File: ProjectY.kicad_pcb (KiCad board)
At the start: 4 copper layers, 192 parts, among them J10 NRJ6HF, J11 NRJ6HF, J2 NRJ6HF, J3 9V, J4 NRJ6HF, J5 NRJ6HF, J6 NRJ6HF, J8 Midi In, J9 MIDI Out, P1 USB_C, Q1 DMT6008LFG, Q2 BC847BS, Q3 BC846BS, Q4 BC856BS, U1 W9825G6KH-6, U10 OPA1692xDGK, U12 USBLC6-2P6, U13 OPA2156xD, U14 OPA1692xDGK, U15 ISOM8115, U16 OPA2156xD, U17 TPS2121RUXR, U18 STM32H7R7I8Tx, U19 TLV77333PDBVR, U20 TPS65133DPDR, U21 LM74700, U22 TLV77325PDBVR, U23 OPA2156xD, U3 FM24CL64B, U4 TPS7A39, U5 OPA2156xD, U6 TAC5242, U7 OPA2156xD, U8 OPA2156xD, U9 OPA2156xD, Y1 ASDLJ-E-49.152MHZ-L-R-T

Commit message: started the layout process
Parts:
- removed C80: 1uF, PCM_JLCPCB:C_0402
- removed D10, D9: BAT54WS, PCM_JLCPCB:D_SOD-323
- removed J11: NRJ6HF, Connector_Audio:Jack_6.35mm_Neutrik_NRJ6HF_Horizontal
- removed P1: USB_C, Connector_USB:USB_C_Receptacle_GCT_USB4110
- removed Q2: BC847BS, PCM_JLCPCB:SOT-363_SC-70-6
- removed Q3: BC846BS, Package_TO_SOT_SMD:SOT-363_SC-70-6
- removed Q4: BC856BS, Package_TO_SOT_SMD:SOT-363_SC-70-6
- added C100: 100nF, PCM_JLCPCB:C_0402, F.Cu at (114.5, 71.4)
- added C101: 100nF, PCM_JLCPCB:C_0402, F.Cu at (114.4, 75.1)
- added C102: 100nF, PCM_JLCPCB:C_0402, F.Cu at (117.8, 75.5)
- added C103: 100nF, PCM_JLCPCB:C_0402, F.Cu at (117.8, 71.2)
- added C104: 100nF, PCM_JLCPCB:C_0402, F.Cu at (111.7, 88.3)
- added C105: 100nF, PCM_JLCPCB:C_0402, F.Cu at (111.7, 92.1)
- added C106: 100uF, PCM_JLCPCB:C_1206, F.Cu at (33.7, 113.6)
- added C107: 100uF, PCM_JLCPCB:C_1206, F.Cu at (33.7, 108.9)
- added C108: 100uF, PCM_JLCPCB:C_1206, F.Cu at (31.3, 108.9)
- added C109: 100uF, PCM_JLCPCB:C_1206, F.Cu at (31.3, 113.6)
- added C110: 100uF, PCM_JLCPCB:C_1206, F.Cu at (28.8, 108.9)
- added C111: 100uF, PCM_JLCPCB:C_1206, F.Cu at (28.8, 113.6)
- added C112: 2.2uF, PCM_JLCPCB:C_0402, F.Cu at (180.6, 162.3)
- added C113: 2.2uF, PCM_JLCPCB:C_0402, F.Cu at (163.2, 165.6)
- added C114: 2.2uF, PCM_JLCPCB:C_0402, F.Cu at (180.7, 143.9)
- added C115: 2.2uF, PCM_JLCPCB:C_0402, F.Cu at (160.3, 136.1)
- added C116: 1uF, PCM_JLCPCB:C_0402, F.Cu at (170.5, 135.6)
- added C117: 100nF, PCM_JLCPCB:C_0402, F.Cu at (170.5, 136.5)
- added C118: 1uF, PCM_JLCPCB:C_0402, F.Cu at (150.7, 139.6)
- added C119: 100nF, PCM_JLCPCB:C_0402, F.Cu at (151.7, 139.6)
- added C120: 4.7uF, PCM_JLCPCB:C_0402, F.Cu at (158.5, 136.1)
- added C121: 100nF, PCM_JLCPCB:C_0402, F.Cu at (161.4, 165.6)
- added C122: 100nF, PCM_JLCPCB:C_0402, F.Cu at (158.2, 165.6)
- added C123: 100nF, PCM_JLCPCB:C_0402, F.Cu at (151.2, 160.1)
- added C124: 100nF, PCM_JLCPCB:C_0402, F.Cu at (151.2, 153.1)
- added C125: 100nF, PCM_JLCPCB:C_0402, F.Cu at (151.3, 145.7)
- added C126: 100nF, PCM_JLCPCB:C_0402, F.Cu at (151.2, 142.1)
- added C127: 1uF, PCM_JLCPCB:C_0402, F.Cu at (88.7, 121.4)
- added C128: 100nF, PCM_JLCPCB:C_0402, F.Cu at (180.6, 160.5)
- added C130: 100nF, PCM_JLCPCB:C_0402, F.Cu at (180.7, 148.1)
- added C132: 100nF, PCM_JLCPCB:C_0402, F.Cu at (180.7, 142.0)
- added C133: 100nF, PCM_JLCPCB:C_0402, F.Cu at (172.7, 136.1)
- added C134: 100nF, PCM_JLCPCB:C_0402, F.Cu at (88.7, 123.2)
- added C135: 4.7uF, PCM_JLCPCB:C_0402, F.Cu at (172.9, 165.1)
- added C136: 100nF, PCM_JLCPCB:C_0402, F.Cu at (172.9, 166.0)
- added C137: 100nF, PCM_JLCPCB:C_0402, F.Cu at (167.2, 165.1)
- added C138: 100nF, PCM_JLCPCB:C_0402, F.Cu at (164.1, 165.6)
- added C139: 4.7uF, PCM_JLCPCB:C_0402, F.Cu at (180.6, 151.1)
- added C140: 100nF, PCM_JLCPCB:C_0402, F.Cu at (180.6, 159.6)
- added C141: 100nF, PCM_JLCPCB:C_0402, F.Cu at (180.6, 156.6)
- added C142: 100nF, PCM_JLCPCB:C_0402, F.Cu at (180.6, 153.6)
- added C143: 100nF, PCM_JLCPCB:C_0402, F.Cu at (180.7, 142.9)
- added C144: 100nF, PCM_JLCPCB:C_0402, F.Cu at (180.6, 161.4)
- added C145: 100nF, PCM_JLCPCB:C_0402, F.Cu at (159.4, 136.1)
- added C146: 100nF, PCM_JLCPCB:C_0402, F.Cu at (162.3, 165.6)
- added C147: 10uF, PCM_JLCPCB:C_0603, F.Cu at (114.0, 133.0)
- added C148: 4.7uF, PCM_JLCPCB:C_0402, F.Cu at (91.5, 112.2)
- added C149: 2.2uF, PCM_JLCPCB:C_0402, F.Cu at (91.5, 114.0)
- added C150: 2.2uF, PCM_JLCPCB:C_0402, F.Cu at (91.5, 115.8)
- added C151: 2.2uF, PCM_JLCPCB:C_0402, F.Cu at (91.5, 117.7)
- added C152: 2.2uF, PCM_JLCPCB:C_0402, F.Cu at (91.5, 119.5)
- added C153: 10uF, PCM_JLCPCB:C_0603, F.Cu at (114.0, 135.2)
- added C154: 220pF, PCM_JLCPCB:C_0402, F.Cu at (151.3, 146.6)
- added C155: 100nF, PCM_JLCPCB:C_0402, F.Cu at (150.4, 148.1)
- added C53: 100uF, PCM_JLCPCB:C_1206, F.Cu at (38.6, 113.6)
- added C56: 100uF, PCM_JLCPCB:C_1206, F.Cu at (38.6, 108.9)
- added C66: 10nF, PCM_JLCPCB:C_0402, F.Cu at (27.0, 113.1)
- added C67: 100nF, PCM_JLCPCB:C_0402, F.Cu at (185.2, 150.6)
- added C74: 2.2nF, PCM_JLCPCB:C_0805, F.Cu at (119.1, 141.7)
- added C75: 2.2nF, PCM_JLCPCB:C_0805, F.Cu at (119.1, 147.8)
- added C76: 100nF, PCM_JLCPCB:C_0402, F.Cu at (164.7, 136.2)
- added C77: 100nF, PCM_JLCPCB:C_0402, F.Cu at (112.8, 185.9)
- added C88: 100nF, PCM_JLCPCB:C_0402, F.Cu at (85.8, 115.8)
- added C89: 100nF, PCM_JLCPCB:C_0402, F.Cu at (85.8, 117.7)
- added C90: 100nF, PCM_JLCPCB:C_0402, F.Cu at (85.8, 119.5)
- added C91: 100nF, PCM_JLCPCB:C_0402, F.Cu at (85.8, 121.4)
- added C92: 100nF, PCM_JLCPCB:C_0402, F.Cu at (85.8, 123.2)
- added C93: 100nF, PCM_JLCPCB:C_0402, F.Cu at (85.8, 125.1)
- added C94: 100pF, PCM_JLCPCB:C_0402, F.Cu at (39.3, 71.8)
- added C96: 10uF, PCM_JLCPCB:C_0402, F.Cu at (72.2, 192.2)
- added C97: 100nF, PCM_JLCPCB:C_0402, F.Cu at (113.4, 73.3)
- added C98: 100nF, PCM_JLCPCB:C_0402, F.Cu at (110.7, 90.3)
- added C99: 100nF, PCM_JLCPCB:C_0402, F.Cu at (85.8, 134.3)
- added D19: BAV99, Package_TO_SOT_SMD:SOT-23, F.Cu at (43.7, 71.9)
- added D2: SMF6.0CA, PCM_JLCPCB:D_SOD-123FL, F.Cu at (97.9, 168.7)
- added NT1: ~, NetTie:NetTie-2_SMD_Pad0.5mm, F.Cu at (115.9, 156.4)
- added NT10: ~, NetTie:NetTie-2_SMD_Pad0.5mm, F.Cu at (115.9, 168.4)
- added NT3: ~, NetTie:NetTie-2_SMD_Pad0.5mm, F.Cu at (115.9, 157.9)
- added NT4: ~, NetTie:NetTie-2_SMD_Pad0.5mm, F.Cu at (115.9, 159.4)
- added NT5: ~, NetTie:NetTie-2_SMD_Pad0.5mm, F.Cu at (115.9, 160.9)
- added NT6: ~, NetTie:NetTie-2_SMD_Pad0.5mm, F.Cu at (115.9, 162.4)
- added NT7: ~, NetTie:NetTie-2_SMD_Pad0.5mm, F.Cu at (115.9, 163.9)
- added NT8: ~, NetTie:NetTie-2_SMD_Pad0.5mm, F.Cu at (115.9, 165.4)
- added NT9: ~, NetTie:NetTie-2_SMD_Pad0.5mm, F.Cu at (115.9, 166.9)
- added Q6: BC847, Package_TO_SOT_SMD:SOT-23, F.Cu at (104.8, 144.2)
- added Q7: BC847, Package_TO_SOT_SMD:SOT-23, F.Cu at (104.8, 148.8)
- added Q8: BC847, Package_TO_SOT_SMD:SOT-23, F.Cu at (104.8, 153.4)
- added Q9: BC847, Package_TO_SOT_SMD:SOT-23, F.Cu at (104.8, 158.0)
- added R100: 10kΩ, PCM_JLCPCB:R_0402, F.Cu at (100.1, 127.0)
- added R101: 1kΩ, PCM_JLCPCB:R_0805, F.Cu at (100.1, 153.3)
- added R102: 1kΩ, PCM_JLCPCB:R_0805, F.Cu at (100.1, 156.3)
- added R103: 10kΩ, PCM_JLCPCB:R_0402, F.Cu at (100.1, 128.8)
- added R104: 100Ω, PCM_JLCPCB:R_0402, F.Cu at (115.8, 70.7)
- added R105: 100Ω, PCM_JLCPCB:R_0402, F.Cu at (115.8, 76.0)
- added R106: 100Ω, PCM_JLCPCB:R_0402, F.Cu at (116.7, 76.0)
- added R107: 100Ω, PCM_JLCPCB:R_0402, F.Cu at (116.8, 70.8)
- added R108: 100Ω, PCM_JLCPCB:R_0402, F.Cu at (115.0, 88.5)
- added R109: 100Ω, PCM_JLCPCB:R_0402, F.Cu at (115.0, 92.0)
- added R110: 10kΩ, PCM_JLCPCB:R_0402, F.Cu at (113.4, 72.4)
- added R111: 10kΩ, PCM_JLCPCB:R_0402, F.Cu at (113.4, 74.2)
- added R112: 10kΩ, PCM_JLCPCB:R_0402, F.Cu at (118.7, 73.8)
- added R113: 10kΩ, PCM_JLCPCB:R_0402, F.Cu at (118.7, 72.6)
- added R114: 10kΩ, PCM_JLCPCB:R_0402, F.Cu at (110.7, 89.3)
- added R115: 10kΩ, PCM_JLCPCB:R_0402, F.Cu at (110.7, 91.2)
- added R116: 1kΩ, PCM_JLCPCB:R_0402, F.Cu at (188.4, 146.2)
- added R117: 10kΩ, PCM_JLCPCB:R_0402, F.Cu at (102.9, 128.8)
- added R118: 100Ω, PCM_JLCPCB:R_0402, F.Cu at (32.6, 69.5)
- added R35: 33Ω, PCM_JLCPCB:R_0402, F.Cu at (94.4, 117.7)
- added R40: 33Ω, PCM_JLCPCB:R_0402, F.Cu at (94.4, 125.1)
- added R45: 33Ω, PCM_JLCPCB:R_0402, F.Cu at (94.4, 130.7)
- added R59: R, Resistor_SMD:R_0402_1005Metric, F.Cu at (25.9, 109.2)
- added R61: R, Resistor_SMD:R_0402_1005Metric, F.Cu at (25.9, 113.1)
- added R74: 10kΩ, PCM_JLCPCB:R_0402, F.Cu at (97.2, 119.5)
- added R75: 510Ω, PCM_JLCPCB:R_0805, F.Cu at (158.1, 45.3)
- added R78: 10kΩ, PCM_JLCPCB:R_0402, F.Cu at (97.2, 123.2)
- added R82: 510Ω, PCM_JLCPCB:R_0805, F.Cu at (134.3, 42.9)
- added R83: 510Ω, PCM_JLCPCB:R_0805, F.Cu at (134.3, 45.8)
- added R84: 10kΩ, PCM_JLCPCB:R_0402, F.Cu at (97.2, 127.0)
- added R85: 10kΩ, PCM_JLCPCB:R_0402, F.Cu at (97.2, 130.7)
- added R86: 10kΩ, PCM_JLCPCB:R_0402, F.Cu at (97.2, 134.3)
- added R87: 10kΩ, PCM_JLCPCB:R_0402, F.Cu at (100.1, 112.2)
- added R88: 10kΩ, PCM_JLCPCB:R_0805, F.Cu at (162.8, 23.5)
- added R89: 10kΩ, PCM_JLCPCB:R_0805, F.Cu at (162.8, 27.1)
- added R90: 10kΩ, PCM_JLCPCB:R_0805, F.Cu at (134.3, 48.8)
- added R91: 10kΩ, PCM_JLCPCB:R_0805, F.Cu at (134.3, 51.7)
- added R92: 10kΩ, PCM_JLCPCB:R_0402, F.Cu at (100.1, 115.8)
- added R93: 10kΩ, PCM_JLCPCB:R_0402, F.Cu at (100.1, 117.7)
- added R94: 10kΩ, PCM_JLCPCB:R_0402, F.Cu at (100.1, 119.5)
- added R95: 10kΩ, PCM_JLCPCB:R_0402, F.Cu at (100.1, 121.4)
- added R96: 10kΩ, PCM_JLCPCB:R_0402, F.Cu at (100.1, 123.2)
- added R97: 10kΩ, PCM_JLCPCB:R_0402, F.Cu at (100.1, 125.1)
- added R99: 1MΩ, PCM_JLCPCB:R_0805, F.Cu at (40.8, 72.5)
- added U2: W25Q128JVS, Package_SO:SOIC-8_5.3x5.3mm_P1.27mm, F.Cu at (167.2, 170.5)
- added U24: OPA1692xDGK, Package_SO:VSSOP-8_3x3mm_P0.65mm, F.Cu at (86.6, 34.0)
- added U25: TLV9004xRUCR, Package_DFN_QFN:Texas_S-PX2QFN-14, F.Cu at (116.0, 73.4)
- added U26: TLV9004xRUCR, Package_DFN_QFN:Texas_S-PX2QFN-14, F.Cu at (113.4, 90.3)
- added U27: TLV77333PDBVR, Package_TO_SOT_SMD:SOT-23-5, F.Cu at (69.5, 192.5)
- C53, C56: footprint PCM_JLCPCB:C_CASE-B-3528-21(mm) -> PCM_JLCPCB:C_1206
- C6: footprint PCM_JLCPCB:C_0603 -> PCM_JLCPCB:C_0402
- C74, C75: value 1uF -> 2.2nF; footprint PCM_JLCPCB:C_0402 -> PCM_JLCPCB:C_0805
- C76, C77: value 1uF -> 100nF
- C78: value 1uF -> 10uF
- C79: value 1uF -> 10nF
- J2: value NRJ6HF -> Conn_ARM_JTAG_SWD_10; footprint Connector_Audio:Jack_6.35mm_Neutrik_NRJ6HF_Horizontal -> Connector_PinHeader_1.27mm:PinHeader_2x05_P1.27mm_Vertical_SMD
- J9: value MIDI Out -> USB_C_Receptacle_USB2.0_14P; footprint Connector_Audio:Jack_3.5mm_Lumberg_1503_07_Horizontal -> Connector_USB:USB_C_Receptacle_GCT_USB4110
- R13, R14, R16, R80, R81: footprint PCM_JLCPCB:R_0805 -> PCM_JLCPCB:R_0402
- R2: value 1MΩ -> 220Ω; footprint PCM_JLCPCB:R_0402 -> PCM_JLCPCB:R_0805
- R30: value 120Ω -> 100kΩ
- R35: value 120Ω -> 33Ω
- R4: value 1MΩ -> 100kΩ
- R40, R45: value 10kΩ -> 33Ω
- R74, R78: value 1kΩ -> 10kΩ; footprint PCM_JLCPCB:R_0805 -> PCM_JLCPCB:R_0402
- R75, R79: value 1kΩ -> 510Ω
- R84, R85, R86, R87: value 100kΩ -> 10kΩ; footprint PCM_JLCPCB:R_0805 -> PCM_JLCPCB:R_0402
- U1: moved to B.Cu
- U13, U16, U23, U5, U8, U9: footprint Package_SO:SOIC-8_3.9x4.9mm_P1.27mm -> Package_SO:VSSOP-8_3x3mm_P0.65mm
- U7: value OPA2156xD -> 74HC14
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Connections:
- net /Analog Audio/IN_R+ renamed /IN_R+
- net /Analog Audio/IN_R- renamed /IN_R-
- net /Analog Audio/Line_Output_L+ renamed /Line_Output_L+
- net /Analog Audio/Line_Output_L- renamed /Line_Output_L-
- net /Analog Audio/~{Dry_Through} renamed /Analog Audio/Dry_Through
- net /Analog Audio/~{Hi-Z} renamed /Analog Audio/Hi-Z
- net Net-(K2-Pad3) renamed Processing_In_Right
- net Net-(K2-Pad6) renamed Processing_In_Left
- net Net-(R18-Pad2) renamed Processing_Inverted_Right
- net Net-(R22-Pad1) renamed Processing_Inverted_Left
- net Net-(U5B--) renamed Summing_In_L
- net Net-(U9A--) renamed Unbal_Left
- net Net-(U9B--) renamed Unbal_Right
- C38 pad 1: Net-(U7A-+) -> Net-(U24A-+)
- C38 pad 2: Net-(U7A--) -> Net-(U24A--)
- C39 pad 1: Net-(U7A-+) -> Net-(U24A-+)
- C39 pad 2: Net-(U7A--) -> Net-(U24A--)
- C44 pad 1: Net-(U7B-+) -> Net-(U24B-+)
- C44 pad 2: Net-(U7B--) -> Net-(U24B--)
- C45 pad 1: Net-(U7B-+) -> Net-(U24B-+)
- C45 pad 2: Net-(U7B--) -> Net-(U24B--)
- C53 pad 1: /Analog Audio/+4.5V -> GND
- C53 pad 2: GND -> /Analog Audio/-4.5V
- C56 pad 1: GND -> /Analog Audio/+4.5V
- C56 pad 2: /Analog Audio/-4.5V -> GND
- C69 pad 1: /PSU/+2.5VA -> /DSP/2.5V_VREF
- C74 pad 1: /MIDI + UI/MIDI IN Shield -> GND
- C74 pad 2: GND -> /Line_Output_R+
- C75 pad 1: /MIDI + UI/MIDI IN Shield -> GND
- C75 pad 2: GND -> /Line_Output_R-
- C76 pad 1: /MIDI + UI/MIDI IN Shield -> VDD
- C77 pad 1: /MIDI + UI/MIDI OUT Shield -> VDD
- C78 pad 1: /MIDI + UI/MIDI OUT Shield -> /PSU/+5V
- C79 pad 1: /MIDI + UI/MIDI OUT Shield -> /Analog Audio/+4.5V
- C79 pad 2: GND -> FBP
- D11 pad 3: /Analog Audio/Guitar_IN -> Buffer_In_Left
- D14 pad 3: /Analog Audio/Line_Output_R+ -> /Line_Output_R+
- D15 pad 3: /Analog Audio/Line_Output_R- -> /Line_Output_R-
- D16 pad 3: /Analog Audio/IN_L+ -> Balun_In_Left+
- D8 pad 3: /Analog Audio/IN_L- -> Balun_In_Left-
- J4 pad R: /Analog Audio/Line_Output_R- -> /Line_Output_R-
- J4 pad T: /Analog Audio/Line_Output_R+ -> /Line_Output_R+
- J6 pad R: /Analog Audio/IN_L- -> /IN_L-
- J6 pad T: /Analog Audio/IN_L+ -> /IN_L+
- R13 pad 1: /Analog Audio/Guitar_IN -> Buffer_In_Right
- R13 pad 2: Net-(U9A-+) -> Net-(U9B-+)
- R14 pad 1: /Analog Audio/IN_L- -> Balun_In_Left-
- R16 pad 1: /Analog Audio/IN_L+ -> Balun_In_Left+
- R2 pad 1: /MIDI + UI/MIDI IN Shield -> /MIDI + UI/Midi In Sink
- R2 pad 2: GND -> Net-(R2-Pad2)
- R26 pad 2: Net-(U7A--) -> Net-(U24A--)
- R27 pad 2: Net-(U7A-+) -> Net-(U24A-+)
- R28 pad 2: Net-(U7B--) -> Net-(U24B--)
- R29 pad 2: Net-(U7B-+) -> Net-(U24B-+)
- R30 pad 1: Net-(Q3A-E1) -> +3.3VA2_Midpoint
- R35 pad 1: /Analog Audio/+3.3V -> Net-(U18-PA13(JTMS)
- R35 pad 2: Net-(Q4A-E1) -> /DSP/SWDIO
- R4 pad 1: /MIDI + UI/MIDI OUT Shield -> /MIDI + UI/+3.3VA2
- R4 pad 2: GND -> +3.3VA2_Midpoint
- R40 pad 1: Net-(Q4A-B1) -> Net-(U18-PA14(JTCK)
- R40 pad 2: GND -> /DSP/SWCLK
- R45 pad 1: /DSP/MIDI_UART0_TX -> Net-(U18-PB3(JTDO)
- R45 pad 2: Net-(Q3A-B1) -> /DSP/SWO
- R74 pad 1: GND -> /Analog Audio/+3.3V
- R74 pad 2: Net-(U16B-+) -> Net-(J1-Pin_1)
- R75 pad 1: GND -> Net-(U16A--)
- R75 pad 2: Net-(U16A-+) -> Balun_Left
- R78 pad 1: Net-(U16B--) -> Net-(J1-Pin_1)
- R78 pad 2: Net-(K2-Pad4) -> Net-(C88-Pad1)
- R79 pad 1: Net-(U16A--) -> GND
- R79 pad 2: Net-(K2-Pad5) -> Net-(U16A-+)
- R84 pad 1: Net-(U13A-+) -> /Analog Audio/+3.3V
- R84 pad 2: GND -> Net-(J12-Pin_1)
- R85 pad 1: GND -> Net-(J12-Pin_1)
- R85 pad 2: Net-(U13B-+) -> Net-(C89-Pad1)
- R86 pad 1: Net-(U23A-+) -> /Analog Audio/+3.3V
- R86 pad 2: GND -> Net-(J13-Pin_1)
- R87 pad 1: GND -> Net-(J13-Pin_1)
- R87 pad 2: Net-(U23B-+) -> Net-(C90-Pad1)
- U1 pad 12: GNDD -> GND
- U1 pad 28: GNDD -> GND
- U1 pad 41: GNDD -> GND
- U1 pad 46: GNDD -> GND
- U1 pad 52: GNDD -> GND
- U1 pad 54: GNDD -> GND
- U1 pad 6: GNDD -> GND
- U15 pad 2: /MIDI + UI/Midi In Sink -> Net-(R2-Pad2)
- U16 pad 1: Net-(K2-Pad5) -> Balun_Left
- U16 pad 7: Net-(K2-Pad4) -> Balun_Right
- U18 pad 1: /DSP/VTREF -> VBAT
- U18 pad 105: unconnected-(U18-VDDXSPI2-Pad105) -> VDDXSPI2
- U18 pad 110: unconnected-(U18-VDDXSPI2-Pad110) -> VDDXSPI2
- U18 pad 116: /DSP/VTREF -> VDD
- U18 pad 12: /DSP/VTREF -> VDD
- U18 pad 121: /DSP/MIDI_UART0_TX -> unconnected-(U18-PA12-Pad121)
- U18 pad 122: /DSP/SWDIO -> Net-(U18-PA13(JTMS)
- U18 pad 123: /DSP/SWCLK -> Net-(U18-PA14(JTCK)
- U18 pad 125: unconnected-(U18-VCAP3-Pad125) -> VCAP
- U18 pad 127: unconnected-(U18-VDDLDO-Pad127) -> VDDLDO
- U18 pad 128: /DSP/VTREF -> VDD
- U18 pad 14: unconnected-(U18-VLXSMPS-Pad14) -> VLXSMPS
- U18 pad 141: /DSP/VTREF -> VDD
- U18 pad 146: unconnected-(U18-VDD50USB-Pad146) -> VDD33USB
- U18 pad 147: unconnected-(U18-VDD33USB-Pad147) -> VDD33USB
- U18 pad 15: unconnected-(U18-VDDSMPS-Pad15) -> VDDSMPS
- U18 pad 157: /DSP/VTREF -> VDD
- U18 pad 16: unconnected-(U18-VFBSMPS-Pad16) -> VCAP
- U18 pad 163: /DSP/SWO -> Net-(U18-PB3(JTDO)
- U18 pad 166: unconnected-(U18-VCAP4-Pad166) -> VCAP
- U18 pad 168: unconnected-(U18-VDDLDO-Pad168) -> VDDLDO
- U18 pad 169: /DSP/VTREF -> VDD
- U18 pad 27: /DSP/VTREF -> VDD
- U18 pad 33: unconnected-(U18-VREFM-Pad33) -> GND
- U18 pad 35: unconnected-(U18-VDDA-Pad35) -> VDDA
- U18 pad 41: /DSP/VTREF -> VDD
- U18 pad 5: /DSP/VTREF -> VDD
- U18 pad 51: /DSP/VTREF -> VDD
- U18 pad 58: /DSP/VTREF -> VDD
- U18 pad 59: unconnected-(U18-VDDLDO-Pad59) -> VDDLDO
- U18 pad 61: unconnected-(U18-VCAP1-Pad61) -> VCAP
- U18 pad 63: unconnected-(U18-VDDXSPI1-Pad63) -> VDDXSPI1
- U18 pad 69: unconnected-(U18-VDDXSPI1-Pad69) -> VDDXSPI1
- U18 pad 75: unconnected-(U18-VDDXSPI1-Pad75) -> VDDXSPI1
- U18 pad 81: unconnected-(U18-VDDXSPI1-Pad81) -> VDDXSPI1
- U18 pad 89: unconnected-(U18-VCAP2-Pad89) -> VCAP
- U18 pad 91: unconnected-(U18-VDDLDO-Pad91) -> VDDLDO
- U18 pad 92: /DSP/VTREF -> VDD
- U18 pad 93: unconnected-(U18-VDDXSPI2-Pad93) -> VDDXSPI2
- U18 pad 99: unconnected-(U18-VDDXSPI2-Pad99) -> VDDXSPI2
- U22 pad 5: /PSU/+2.5VA -> /DSP/2.5V_VREF
- U7 pad 1: Net-(R3-Pad2) -> Net-(C88-Pad1)
- U7 pad 2: Net-(U7A--) -> /DSP/Footswitch_1
- U7 pad 3: Net-(U7A-+) -> Net-(C89-Pad1)
- U7 pad 4: /Analog Audio/-4.5V -> /DSP/Footswitch_2
- U7 pad 5: Net-(U7B-+) -> Net-(C90-Pad1)
- U7 pad 6: Net-(U7B--) -> /DSP/Switch_1A
- U7 pad 7: Net-(R64-Pad2) -> GND
- U7 pad 8: /Analog Audio/+4.5V -> /DSP/Switch_1B
- U9 pad 5: Net-(U9A-+) -> Net-(U9B-+)
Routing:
- net Net-(U18-PH0): track 0.00 -> 2.12 mm
- net /PSU/D-: track 0.00 -> 1.98 mm
- net /PSU/D+: track 0.00 -> 1.97 mm
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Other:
- board outline added: 110 x 85 mm

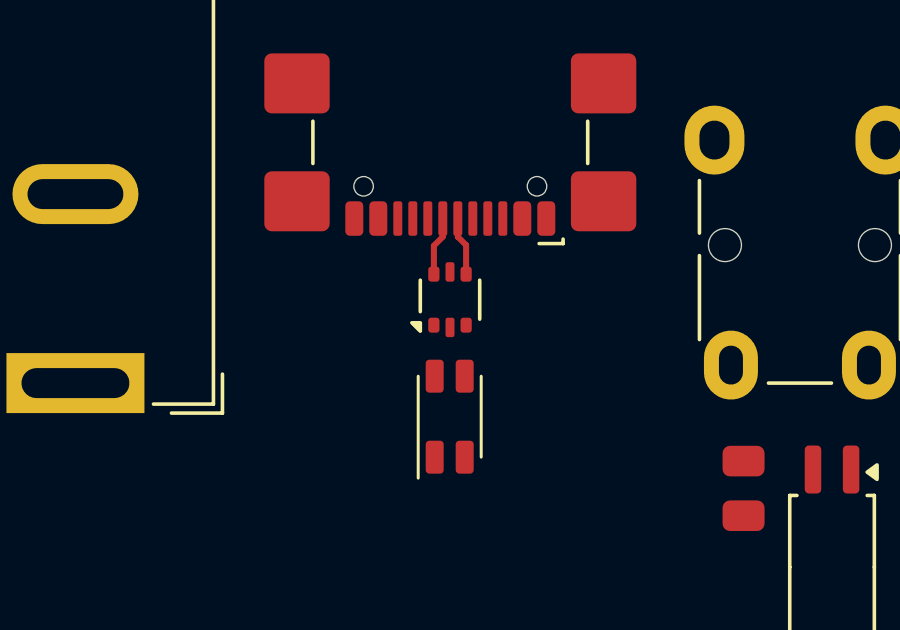
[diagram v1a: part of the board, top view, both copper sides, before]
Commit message: 3v3 dcdc update
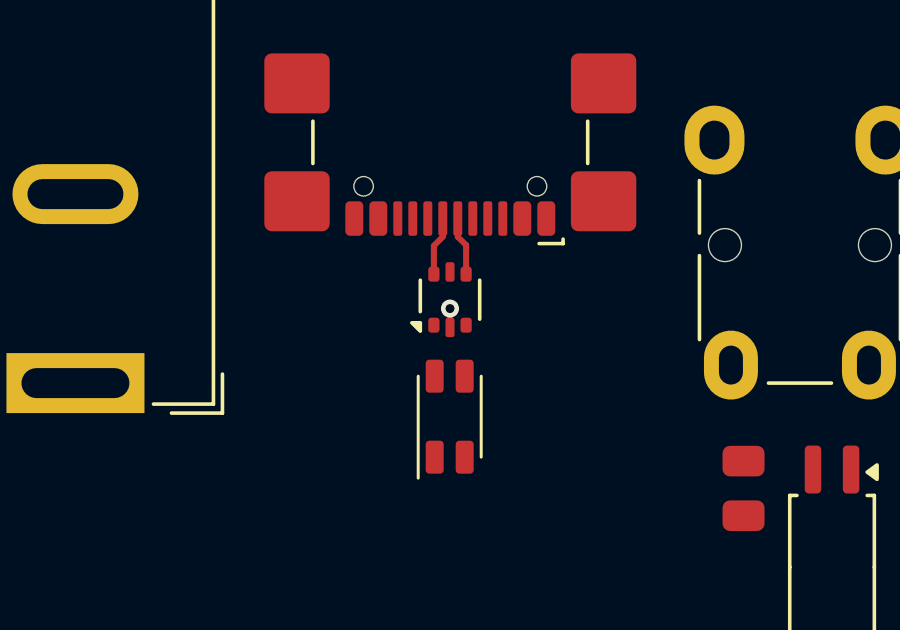
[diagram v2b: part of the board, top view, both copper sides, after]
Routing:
- net GND: track 0.00 -> 0.63 mm, vias 0 -> 1
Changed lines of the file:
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@@
+	)
+	(segment
+		(start 161.015 105.9944)
+		(end 161.015 105.366161)
+		(width 0.2)
+		(layer "F.Cu")
+		(net 1)
+	)
+	(via
+		(at 161.015 105.366161)
+		(size 0.6)
+		(drill 0.3)
+		(layers "F.Cu" "B.Cu")
+		(net 1)
 	)
 	(segment

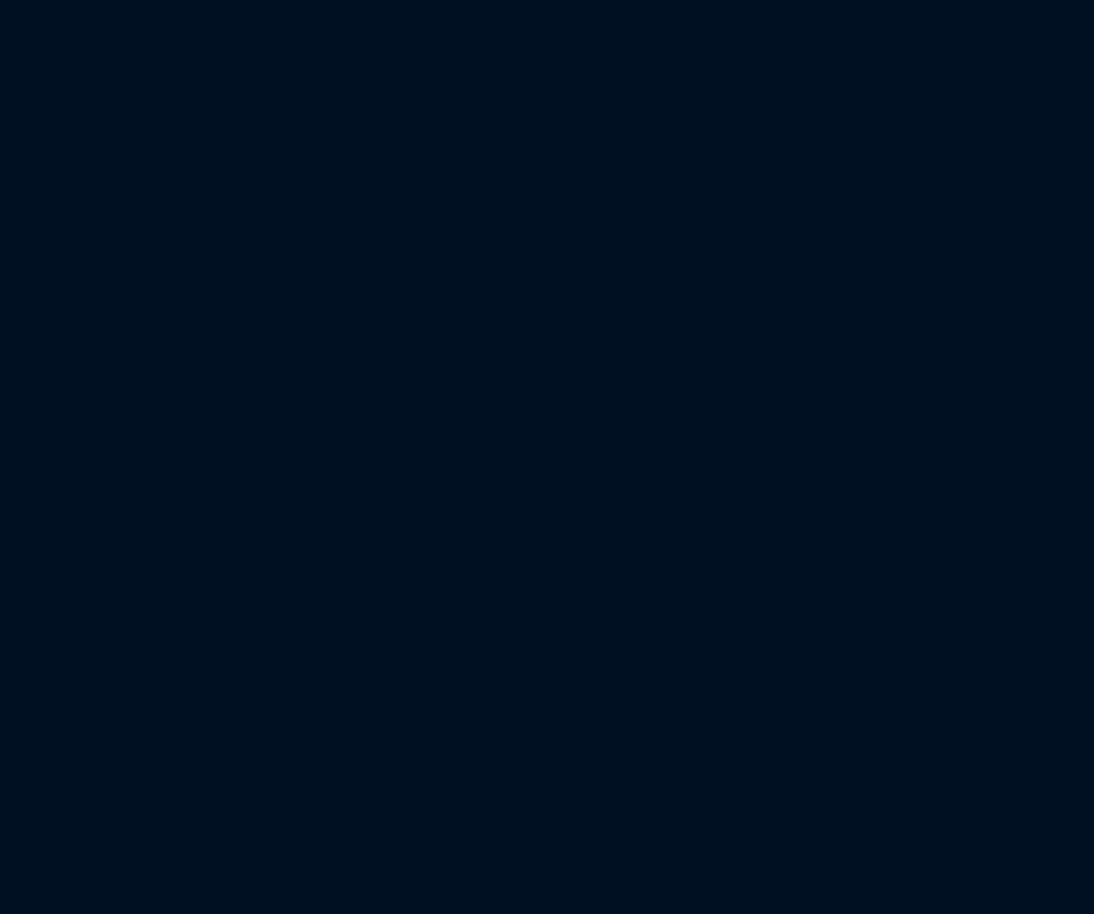
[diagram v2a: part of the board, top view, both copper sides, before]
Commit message: deleted usb powering option because of 4.5V minimum input voltage of DC-DC
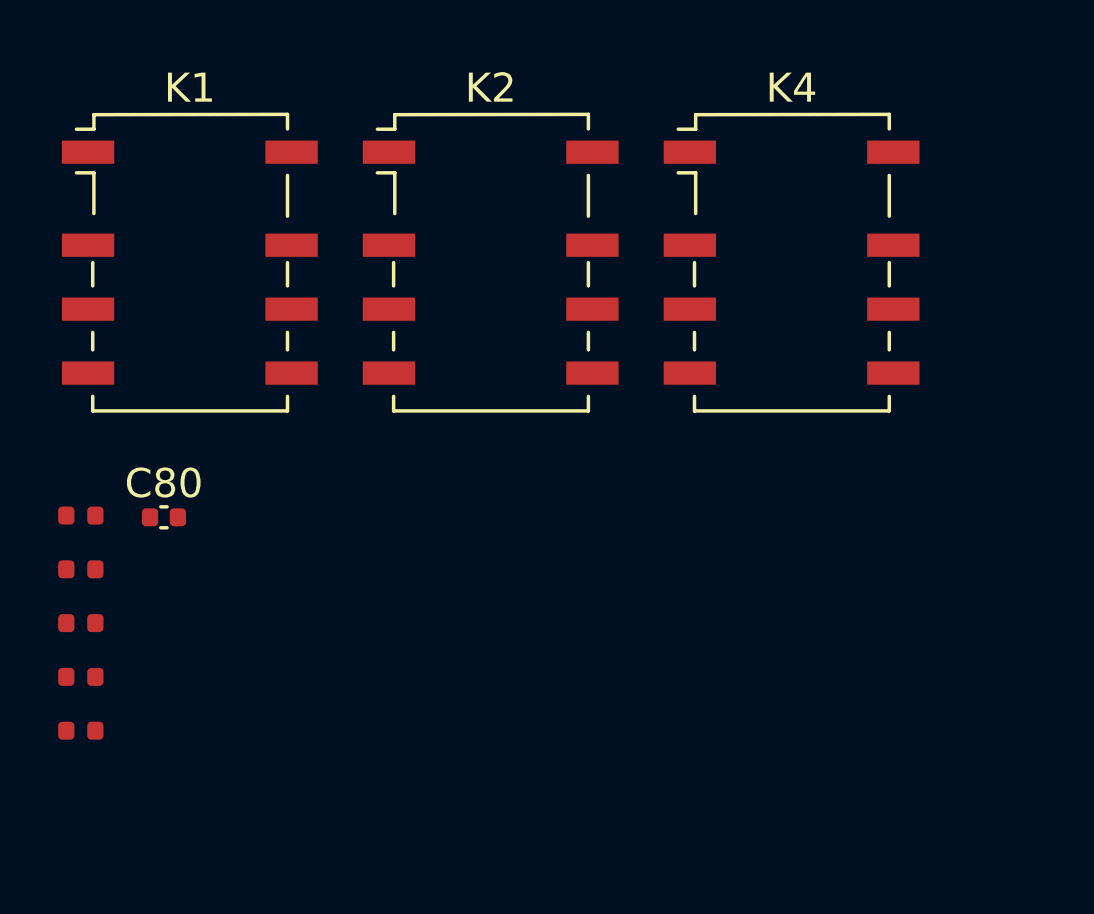
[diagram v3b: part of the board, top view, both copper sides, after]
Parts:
- added C80: C, Capacitor_SMD:C_0402_1005Metric, F.Cu at (3.79, 14.0)
- added C95: 1uF, PCM_JLCPCB:C_0402, F.Cu at (0.93, 14.0)
- added K1: G6K-2, Relay_SMD:Relay_DPDT_Omron_G6K-2F-Y, F.Cu at (4.67, 5.28)
- added K2: G6K-2, Relay_SMD:Relay_DPDT_Omron_G6K-2F-Y, F.Cu at (15.0, 5.28)
- added K4: G6K-2, Relay_SMD:Relay_DPDT_Omron_G6K-2F-Y, F.Cu at (25.4, 5.28)
- added R119: 47Ω, PCM_JLCPCB:R_0402, F.Cu at (0.93, 17.7)
- added R120: 24kΩ, PCM_JLCPCB:R_0402, F.Cu at (0.93, 19.5)
- added R121: 100kΩ, PCM_JLCPCB:R_0402, F.Cu at (0.93, 21.4)
- added R98: 75kΩ, PCM_JLCPCB:R_0402, F.Cu at (0.93, 15.8)

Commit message: lot of changes
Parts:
- removed C1, C11, C12, C15, C16, C17, C18, C19, C2, C20, C31, C32, C70, C71, C72, C8, C81, C82, C83, C84, C97, C98: 100nF, PCM_JLCPCB:C_0402
- removed C13, C23, C95: 1uF, PCM_JLCPCB:C_0402
- removed C21, C22, C60, C61, C62, C78, C96: 10uF, PCM_JLCPCB:C_0402
- removed C34, C86, C87, C94: 100pF, PCM_JLCPCB:C_0402
- removed C36, C37, C38, C39, C44, C45, C74 (x2), C75 (x2): 2.2nF, PCM_JLCPCB:C_0805
- removed the C53 at (36.2, 113.6)
- removed the C53 at (38.6, 113.6)
- removed the C56 at (36.2, 108.9)
- removed the C56 at (38.6, 108.9)
- removed the C76 at (83.0, 125.1)
- removed the C77 at (112.8, 185.9)
- removed the C77 at (83.0, 127.0)
- removed D11, D12, D13, D14, D15, D16, D17, D18, D19, D8: BAV99, Package_TO_SOT_SMD:SOT-23
- removed J10, J4: NRJ6HF, Connector_Audio:Jack_6.35mm_Neutrik_NRJ6HF_Horizontal
- removed J8: Midi In, Connector_Audio:Jack_3.5mm_Lumberg_1503_07_Horizontal
- removed K1, K2, K4: G6K-2, Relay_SMD:Relay_DPDT_Omron_G6K-2F-Y
- removed L5: XFL4020-472MEC, Inductor_SMD:L_Coilcraft_XxL4020
- removed Q1: DMT6008LFG, Package_SON:Diodes_PowerDI3333-8
- removed Q6, Q7, Q8, Q9: BC847, Package_TO_SOT_SMD:SOT-23
- removed R100, R103, R110, R111, R112, R113, R114, R115, R57, R68, R71: 10kΩ, PCM_JLCPCB:R_0402
- removed R101, R102, R20, R21, R22, R23, R26, R27, R28, R29, R62, R63, R64, R65, R66, R67, R72, R73, R76, R77: 1kΩ, PCM_JLCPCB:R_0805
- removed R104, R105, R106, R107, R108, R109, R118, R13, R14, R16, R80, R81: 100Ω, PCM_JLCPCB:R_0402
- removed R121: 100kΩ, PCM_JLCPCB:R_0402
- removed R17, R18: 2.2kΩ, PCM_JLCPCB:R_0805
- removed R24, R25, R69, R70: 100Ω, PCM_JLCPCB:R_0805
- removed the R35 at (94.4, 117.7)
- removed the R35 at (94.4, 119.5)
- removed the R40 at (94.4, 127.0)
- removed the R40 at (94.4, 125.1)
- removed the R45 at (94.4, 130.7)
- removed the R45 at (94.4, 128.8)
- removed R48, R51, R53, R55: 4.7kΩ, PCM_JLCPCB:R_0603
- removed the R74 at (97.2, 119.5)
- removed the R74 at (97.2, 121.4)
- removed R75 (x2), R79, R82, R83: 510Ω, PCM_JLCPCB:R_0805
- removed the R78 at (97.2, 123.2)
- removed the R78 at (97.2, 125.1)
- removed R8, R99: 1MΩ, PCM_JLCPCB:R_0805
- removed the R84 at (97.2, 128.8)
- removed the R84 at (97.2, 127.0)
- removed the R85 at (97.2, 130.7)
- removed the R85 at (97.2, 132.5)
- removed the R86 at (97.2, 134.3)
- removed the R86 at (97.2, 136.2)
- removed the R87 at (100.1, 114.0)
- removed the R87 at (100.1, 112.2)
- removed R88, R89, R90, R91: 10kΩ, PCM_JLCPCB:R_0805
- removed U13, U16, U23, U8, U9: OPA2156xD, Package_SO:VSSOP-8_3x3mm_P0.65mm
- removed U17: TPS2121RUXR, User:IC_TPS2121RUXR
- removed U19, U27: TLV77333PDBVR, Package_TO_SOT_SMD:SOT-23-5
- removed U20: TPS65133DPDR, User:SON40P300X300X80-13N
- removed U21: LM74700, Package_TO_SOT_SMD:SOT-23-6
- removed U24: OPA1692xDGK, Package_SO:VSSOP-8_3x3mm_P0.65mm
- removed U25, U26: TLV9004xRUCR, Package_DFN_QFN:Texas_S-PX2QFN-14
- removed U6: TAC5242, Package_DFN_QFN:VQFN-24-1EP_4x4mm_P0.5mm_EP2.5x2.5mm_ThermalVias
- removed U7: 74HC14, Package_SO:SOIC-8_3.9x4.9mm_P1.27mm
- added C129: 10uF, PCM_JLCPCB:C_0603, F.Cu at (140.6, 145.8)
- added C201: 100pF, PCM_JLCPCB:C_0402, F.Cu at (147.9, 122.5)
- added C202: 100pF, PCM_JLCPCB:C_0402, F.Cu at (156.3, 123.5)
- added C203: 2.2nF, PCM_JLCPCB:C_0805, F.Cu at (54.5, 65.7)
- added C204: 2.2nF, PCM_JLCPCB:C_0805, F.Cu at (54.5, 68.8)
- added C205: 10uF 16V, Capacitor_SMD:C_Elec_5x5.8, F.Cu at (127.1, 197.5)
- added C206: 10uF 16V, Capacitor_SMD:C_Elec_5x5.8, F.Cu at (133.1, 197.5)
- added C207: 10uF 16V, Capacitor_SMD:C_Elec_5x5.8, F.Cu at (138.8, 205.4)
- added C208: 10uF 16V, Capacitor_SMD:C_Elec_5x5.8, F.Cu at (139.1, 197.5)
- added C209: 100nF, PCM_JLCPCB:C_0402, F.Cu at (178.9, 104.8)
- added C210: 100nF, PCM_JLCPCB:C_0402, F.Cu at (182.7, 113.5)
- added C211: 100nF, PCM_JLCPCB:C_0402, F.Cu at (147.9, 124.3)
- added C212: 100nF, PCM_JLCPCB:C_0402, F.Cu at (156.3, 121.7)
- added C213: 100nF, PCM_JLCPCB:C_0402, F.Cu at (50.1, 103.6)
- added C214: 100nF, PCM_JLCPCB:C_0402, F.Cu at (50.1, 105.5)
- added C215: 100nF, PCM_JLCPCB:C_0402, F.Cu at (50.1, 107.3)
- added C216: 100nF, PCM_JLCPCB:C_0402, F.Cu at (53.0, 92.5)
- added C217: 100nF, PCM_JLCPCB:C_0402, F.Cu at (53.0, 94.3)
- added C218: 100nF, PCM_JLCPCB:C_0402, F.Cu at (53.0, 96.2)
- added C219: 100pF, PCM_JLCPCB:C_0402, F.Cu at (53.0, 98.0)
- added C220: 100pF, PCM_JLCPCB:C_0402, F.Cu at (53.0, 99.9)
- added C229: 10uF, PCM_JLCPCB:C_0402, F.Cu at (55.8, 99.9)
- added C230: 1uF, PCM_JLCPCB:C_0402, F.Cu at (55.8, 101.8)
- added C231: 47uF, Capacitor_SMD:C_Elec_6.3x7.7, F.Cu at (188.5, 106.5)
- added C232: 47uF, Capacitor_SMD:C_Elec_6.3x7.7, F.Cu at (188.5, 99.3)
- added C233: 10uF, PCM_JLCPCB:C_0402, F.Cu at (55.8, 103.6)
- added C234: 2.2nF, PCM_JLCPCB:C_0805, F.Cu at (181.7, 101.1)
- added C235: 47uF, Capacitor_SMD:C_Elec_6.3x7.7, F.Cu at (188.5, 120.9)
- added C236: 47uF, Capacitor_SMD:C_Elec_6.3x7.7, F.Cu at (188.5, 113.7)
- added C237: 2.2nF, PCM_JLCPCB:C_0805, F.Cu at (181.7, 103.2)
- added C238: 2.2nF, PCM_JLCPCB:C_0805, F.Cu at (181.0, 115.0)
- added C239: 1uF, PCM_JLCPCB:C_0402, F.Cu at (55.8, 105.5)
- added C240: 2.2nF, PCM_JLCPCB:C_0805, F.Cu at (181.0, 117.2)
- added C27: 2.2nF, PCM_JLCPCB:C_0805, F.Cu at (152.1, 37.6)
- added C28: 100nF, PCM_JLCPCB:C_0402, F.Cu at (149.1, 48.6)
- added C29: DNP, Capacitor_SMD:C_0805_2012Metric, F.Cu at (149.2, 36.3)
- added C30: C, Capacitor_SMD:C_0402_1005Metric, F.Cu at (154.0, 37.9)
- added C53: 100uF, PCM_JLCPCB:C_1206, F.Cu at (109.9, 128.4)
- added C56: 100uF, PCM_JLCPCB:C_1206, F.Cu at (109.9, 131.7)
- added C77: 100nF, PCM_JLCPCB:C_0402, F.Cu at (88.5, 118.4)
- added D201: BAV99, Package_TO_SOT_SMD:SOT-23, F.Cu at (145.0, 123.0)
- added D202: BAV99, Package_TO_SOT_SMD:SOT-23, F.Cu at (159.3, 123.0)
- added D203: BAV99, Package_TO_SOT_SMD:SOT-23, F.Cu at (179.0, 122.2)
- added D204: BAV99, Package_TO_SOT_SMD:SOT-23, F.Cu at (179.7, 97.3)
- added D3: SMF20CA, PCM_JLCPCB:D_SOD-123FL, F.Cu at (234.9, 109.5)
- added J7: MIDI In, User:Jack_6.35mm_Neutrik_NRJ6HF_Horizontal, F.Cu at (196.5, 113.2)
- added R130: 12k, Resistor_SMD:R_0402_1005Metric, F.Cu at (105.5, 128.2)
- added R131: 20k, Resistor_SMD:R_0402_1005Metric, F.Cu at (105.5, 130.2)
- added R201: 100Ω, PCM_JLCPCB:R_0402, F.Cu at (147.9, 121.6)
- added R202: 100Ω, PCM_JLCPCB:R_0402, F.Cu at (156.3, 122.6)
- added R203: 1MΩ, PCM_JLCPCB:R_0402, F.Cu at (147.9, 123.4)
- added R204: 1MΩ, PCM_JLCPCB:R_0402, F.Cu at (156.3, 124.4)
- added R205: 3.3kΩ, PCM_JLCPCB:R_0402, F.Cu at (58.6, 98.0)
- added R206: 3k, PCM_JLCPCB:R_0402, F.Cu at (58.6, 99.9)
- added R207: 1.3k, PCM_JLCPCB:R_0402, F.Cu at (58.6, 101.8)
- added R208: 3.3kΩ, PCM_JLCPCB:R_0402, F.Cu at (58.6, 103.6)
- added R209: 3k, PCM_JLCPCB:R_0402, F.Cu at (58.6, 105.5)
- added R210: 1.3k, PCM_JLCPCB:R_0402, F.Cu at (58.6, 107.3)
- added R211: 3.3kΩ, PCM_JLCPCB:R_0402, F.Cu at (61.5, 92.5)
- added R212: 3.3kΩ, PCM_JLCPCB:R_0402, F.Cu at (61.5, 94.3)
- added R213: 3k, PCM_JLCPCB:R_0402, F.Cu at (61.5, 96.2)
- added R214: 1.3k, PCM_JLCPCB:R_0402, F.Cu at (61.5, 98.0)
- added R215: 3k, PCM_JLCPCB:R_0402, F.Cu at (61.5, 99.9)
- added R216: 1.3k, PCM_JLCPCB:R_0402, F.Cu at (61.5, 101.8)
- added R217: 100Ω, PCM_JLCPCB:R_0805, F.Cu at (58.9, 65.7)
- added R218: 100Ω, PCM_JLCPCB:R_0805, F.Cu at (58.9, 68.6)
- added R219: 100Ω, PCM_JLCPCB:R_0805, F.Cu at (58.9, 71.5)
- added R220: 100Ω, PCM_JLCPCB:R_0805, F.Cu at (58.9, 74.5)
- added R221: 1kΩ, PCM_JLCPCB:R_0402, F.Cu at (180.9, 99.5)
- added R222: 1kΩ, PCM_JLCPCB:R_0402, F.Cu at (182.9, 99.5)
- added R223: 1.65k, Resistor_SMD:R_0402_1005Metric, F.Cu at (182.9, 104.8)
- added R224: 1kΩ, PCM_JLCPCB:R_0402, F.Cu at (179.9, 119.8)
- added R225: 1kΩ, PCM_JLCPCB:R_0402, F.Cu at (181.8, 119.8)
- added R226: 1.65k, Resistor_SMD:R_0402_1005Metric, F.Cu at (181.8, 118.8)
- added R227: 1.65k, Resistor_SMD:R_0402_1005Metric, F.Cu at (180.9, 104.8)
- added R228: 1.65k, Resistor_SMD:R_0402_1005Metric, F.Cu at (179.7, 113.5)
- added R229: 1kΩ, PCM_JLCPCB:R_1206, F.Cu at (178.8, 101.9)
- added R230: 1kΩ, PCM_JLCPCB:R_1206, F.Cu at (178.1, 116.5)
- added R3: 47Ω, PCM_JLCPCB:R_0402, F.Cu at (78.6, 45.1)
- added R35: 33Ω, PCM_JLCPCB:R_0402, F.Cu at (99.9, 94.4)
- added R40: 33Ω, PCM_JLCPCB:R_0402, F.Cu at (99.9, 103.6)
- added R41: 1kΩ, PCM_JLCPCB:R_0402, F.Cu at (99.9, 105.5)
- added R42: 1kΩ, PCM_JLCPCB:R_0402, F.Cu at (99.9, 107.3)
- added R45: 33Ω, PCM_JLCPCB:R_0402, F.Cu at (99.9, 112.9)
- added R6: 4.3kΩ, PCM_JLCPCB:R_0603, F.Cu at (92.1, 52.0)
- added R74: 10kΩ, PCM_JLCPCB:R_0402, F.Cu at (102.8, 111.0)
- added R78: 10kΩ, PCM_JLCPCB:R_0402, F.Cu at (102.8, 112.9)
- added R84: 10kΩ, PCM_JLCPCB:R_0402, F.Cu at (102.8, 116.6)
- added R85: 10kΩ, PCM_JLCPCB:R_0402, F.Cu at (102.8, 118.4)
- added R86: 10kΩ, PCM_JLCPCB:R_0402, F.Cu at (102.8, 120.3)
- added R87: 10kΩ, PCM_JLCPCB:R_0402, F.Cu at (105.6, 92.5)
- added U201: OPA1678, Package_SO:VSSOP-8_3x3mm_P0.65mm, F.Cu at (152.1, 123.0)
- added U202: OPA1678, Package_SO:VSSOP-8_3x3mm_P0.65mm, F.Cu at (21.2, 74.1)
- added U203: OPA1678, Package_SO:VSSOP-8_3x3mm_P0.65mm, F.Cu at (21.2, 80.7)
- added U204: OPA1678, Package_SO:VSSOP-8_3x3mm_P0.65mm, F.Cu at (21.2, 87.3)
- added U205: TAC5242, User:TAC5242, F.Cu at (178.1, 142.8)
- added U206: OPA1678, Package_SO:SOIC-8_3.9x4.9mm_P1.27mm, F.Cu at (180.9, 109.2)
- C14, C64: value 10uF -> 1uF; footprint PCM_JLCPCB:C_0603 -> PCM_JLCPCB:C_0402
- C24: value DNP -> 4.7uF; footprint Capacitor_SMD:C_0805_2012Metric -> PCM_JLCPCB:C_0805
- C25, C58: value 10uF -> 1uF
- C35, C85: value 100pF -> 10uF
- C4: value 100nF -> 1uF
- C57: value 100nF -> 10uF
- C59, C6: value 10uF -> 100nF
- C63: value 2.2nF -> 10uF; footprint PCM_JLCPCB:C_0805 -> PCM_JLCPCB:C_0402
- C80: value C -> 10uF; footprint Capacitor_SMD:C_0402_1005Metric -> PCM_JLCPCB:C_0402
- C9: value 10uF -> 100nF; footprint PCM_JLCPCB:C_0603 -> PCM_JLCPCB:C_0402
- J3: footprint Connector_BarrelJack:BarrelJack_GCT_DCJ200-10-A_Horizontal -> User:BarrelJack_GCT_DCJ200-10-A_Horizontal
- J5: value NRJ6HF -> Out; footprint Connector_Audio:Jack_6.35mm_Neutrik_NRJ6HF_Horizontal -> User:Jack_6.35mm_Neutrik_NRJ6HF_Horizontal
- J6: value NRJ6HF -> IN; footprint Connector_Audio:Jack_6.35mm_Neutrik_NRJ6HF_Horizontal -> User:Jack_6.35mm_Neutrik_NRJ6HF_Horizontal
- J9: footprint Connector_USB:USB_C_Receptacle_GCT_USB4110 -> User:USB_C_Receptacle_GCT_USB4110
- L4: value XFL4020-472MEC -> 3.6uH; footprint Inductor_SMD:L_Coilcraft_XxL4020 -> Inductor_SMD:L_Cenker_CKCS8040
- R10, R11: value 5.1kΩ -> 56kΩ
- R119: value 47Ω -> 110k; footprint PCM_JLCPCB:R_0402 -> Resistor_SMD:R_0402_1005Metric
- R120: value 24kΩ -> 8.2k; footprint PCM_JLCPCB:R_0402 -> Resistor_SMD:R_0402_1005Metric
- R30, R4: value 100kΩ -> 1kΩ
- R31: value 1kΩ -> 24kΩ; footprint PCM_JLCPCB:R_0805 -> PCM_JLCPCB:R_0402
- R32: value 1kΩ -> 100kΩ; footprint PCM_JLCPCB:R_0805 -> PCM_JLCPCB:R_0402
- R33: value 1kΩ -> 22kΩ; footprint PCM_JLCPCB:R_0805 -> PCM_JLCPCB:R_0402
- R34: value 1kΩ -> 47Ω; footprint PCM_JLCPCB:R_0805 -> PCM_JLCPCB:R_0402
- R37, R38: footprint PCM_JLCPCB:R_0805 -> PCM_JLCPCB:R_0402
- R46: value 22kΩ -> 75kΩ
- R47: value 47kΩ -> 24kΩ
- R98: value 75kΩ -> 47Ω
- U1: moved to F.Cu
- U10: value OPA1692xDGK -> RT8293B; footprint Package_SO:VSSOP-8_3x3mm_P0.65mm -> Package_SO:TI_SO-PowerPAD-8
- U14: value OPA1692xDGK -> TPS26400PWPR; footprint Package_SO:VSSOP-8_3x3mm_P0.65mm -> User:PWP0016H-IPC_A
- U5: value OPA2156xD -> TPS560430XFDBVT; footprint Package_SO:VSSOP-8_3x3mm_P0.65mm -> Package_TO_SOT_SMD:SOT-23-6
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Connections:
- net /DSP/MIDI_UART0_RX renamed UART0_RX
- net /DSP/SPDIF_OUT renamed SPDIF_NOT_USED
- net /MIDI + UI/MIDI IN Shield renamed /DSP/MIDI IN Shield
- C100 pad 1: Net-(U25A-+) -> /DSP/Potentiometer_1
- C101 pad 1: Net-(U25B-+) -> /DSP/Potentiometer_2
- C102 pad 1: Net-(U25C-+) -> /DSP/Potentiometer_3
- C103 pad 1: Net-(U25D-+) -> /DSP/Potentiometer_4
- C104 pad 1: Net-(U26A-+) -> /DSP/Potentiometer_5
- C105 pad 1: Net-(U26B-+) -> /DSP/Potentiometer_6
- C106 pad 2: /Analog Audio/-4.5V -> /Analog Audio/-V_OPA
- C107 pad 1: /Analog Audio/+4.5V -> /Analog Audio/+V_OPA
- C108 pad 1: /Analog Audio/+4.5V -> /Analog Audio/+V_OPA
- C109 pad 2: /Analog Audio/-4.5V -> /Analog Audio/-V_OPA
- C110 pad 1: /Analog Audio/+4.5V -> /Analog Audio/+V_OPA
- C111 pad 2: /Analog Audio/-4.5V -> /Analog Audio/-V_OPA
- C14 pad 1: GND -> /DSP/VBUS
- C14 pad 2: /PSU/VBUS -> GND
- C24 pad 1: Net-(U11-COMP) -> GND
- C24 pad 2: GND -> -7V
- C25 pad 1: /Analog Audio/+3.3VA -> Net-(U10-SS/PG)
- C26 pad 1: /PSU/+5V -> Net-(U4-INP)
- C33 pad 2: /PSU/-5V -> -7V
- C35 pad 1: Net-(U13A-+) -> /Analog Audio/+3.3V
- C4 pad 1: /PSU/+9V -> Net-(U14-dVdT)
- C4 pad 2: Net-(U21-VCAP) -> PowerPad
- C41 pad 1: /PSU/+5V -> Net-(U4-INP)
- C42 pad 2: /PSU/-5V -> -7V
- C48 pad 1: /PSU/+5V -> Net-(U4-INP)
- C49 pad 2: /PSU/-5V -> -7V
- C5 pad 1: /PSU/+5V -> Net-(U4-INP)
- C57 pad 1: Net-(U11-BOOT) -> /Analog Audio/+3.3V
- C57 pad 2: Net-(U11-SW) -> GND
- C58 pad 1: /Analog Audio/+3.3V -> Net-(U18-VREFP)
- C59 pad 1: /Analog Audio/+3.3V -> Net-(U18-VREFP)
- C59 pad 2: GND -> unconnected-(C59-Pad2)
- C6 pad 1: /PSU/+5V -> Net-(U5-EN)
- C6 pad 2: GND -> -7V
- C63 pad 1: Net-(C63-Pad1) -> /Analog Audio/+3.3V
- C64 pad 1: Net-(U17-SS) -> VBUS_DETECT
- C66 pad 2: /Analog Audio/-4.5V -> /Analog Audio/-V_OPA
- C69 pad 1: /DSP/2.5V_VREF -> /DSP/+2.5VA
- C7 pad 2: /PSU/-5V -> -7V
- C79 pad 1: /Analog Audio/+4.5V -> /Analog Audio/+V_OPA
- C80 pad 1: Net-(C80-Pad1) -> /Analog Audio/+3.3V
- C80 pad 2: Net-(U11-FB) -> GND
- C85 pad 1: Net-(U13B-+) -> /Analog Audio/+3.3V
- C9 pad 1: /PSU/+9V_REVERSE_PROTECTED -> Net-(U5-CB)
- C9 pad 2: GND -> Net-(U5-SW)
- J5 pad R: /Line_Output_L- -> /Analog Audio/Line_Output_R
- J5 pad T: /Line_Output_L+ -> /Analog Audio/Line_Output_L
- J6 pad R: /IN_L- -> /Analog Audio/IN_R
- J6 pad T: /IN_L+ -> /Analog Audio/IN_L
- J9 pad A4: /PSU/VBUS -> /DSP/VBUS
- J9 pad A5: /PSU/CC -> /DSP/CC
- J9 pad A6: /PSU/D+ -> /DSP/D+
- J9 pad A7: /PSU/D- -> /DSP/D-
- J9 pad A9: /PSU/VBUS -> /DSP/VBUS
- J9 pad B4: /PSU/VBUS -> /DSP/VBUS
- J9 pad B5: /PSU/VCONN -> /DSP/VCONN
- J9 pad B6: /PSU/D+ -> /DSP/D+
- J9 pad B7: /PSU/D- -> /DSP/D-
- J9 pad B9: /PSU/VBUS -> /DSP/VBUS
- L1 pad 1: /DSP/D+ -> D+_filt
- L1 pad 4: /DSP/D- -> D-_filt
- L4 pad 1: GND -> Net-(U10-SW)
- L4 pad 2: Net-(U20-SWN) -> /Analog Audio/+3.3V
- R10 pad 1: GND -> /DSP/CC
- R10 pad 2: /PSU/CC -> GND
- R11 pad 1: GND -> /DSP/VCONN
- R11 pad 2: /PSU/VCONN -> GND
- R119 pad 1: /Analog Audio/+3.3V -> /PSU/+9V
- R119 pad 2: Net-(C80-Pad1) -> Net-(U14-UVLO)
- R12 pad 1: /PSU/VIN_FILT -> +9-18V
- R120 pad 1: Net-(U11-FB) -> Net-(U14-UVLO)
- R120 pad 2: GND -> Net-(U14-OVP)
- R2 pad 1: /MIDI + UI/Midi In Sink -> /DSP/Midi In Sink
- R30 pad 1: +3.3VA2_Midpoint -> Net-(R30-Pad1)
- R30 pad 2: GND -> /DSP/Potentiometer_2
- R31 pad 1: Processing_Inverted_Right -> Net-(U5-FB)
- R31 pad 2: Net-(U14A-+) -> Net-(R3-Pad1)
- R32 pad 1: Net-(U14A-+) -> Net-(U10-VIN)
- R32 pad 2: GND -> Net-(U10-EN)
- R33 pad 1: Processing_In_Right -> Net-(U10-COMP)
- R33 pad 2: Net-(U14B-+) -> Net-(C27-Pad1)
- R34 pad 1: Net-(U14B-+) -> /Analog Audio/+3.3V
- R34 pad 2: GND -> Net-(C30-Pad1)
- R36 pad 1: /PSU/VBUS -> /DSP/VBUS
- R36 pad 2: /DSP/VBUS_detect -> VBUS_DETECT
- R37 pad 2: Net-(U16A--) -> /DSP/Potentiometer_3
- R38 pad 2: Net-(U16A-+) -> /DSP/Potentiometer_4
- R39 pad 1: /DSP/VBUS_detect -> VBUS_DETECT
- R4 pad 1: /MIDI + UI/+3.3VA2 -> Net-(R4-Pad1)
- R4 pad 2: +3.3VA2_Midpoint -> /DSP/Potentiometer_1
- R46 pad 1: Net-(U11-COMP) -> Net-(C30-Pad1)
- R46 pad 2: Net-(C63-Pad1) -> Net-(U10-FB)
- R47 pad 1: Net-(U17-ILIM) -> Net-(U10-FB)
- R59 pad 1: /Analog Audio/+4.5V -> /Analog Audio/+V_OPA
- R61 pad 2: /Analog Audio/-4.5V -> /Analog Audio/-V_OPA
- R98 pad 1: Net-(C80-Pad1) -> /DSP/+2.5VA
- R98 pad 2: Net-(U11-FB) -> Net-(U18-VREFP)
- U10 pad 1: Net-(U10A--) -> Net-(U10-BOOT)
- U10 pad 2: Net-(U10A--) -> Net-(U10-VIN)
- U10 pad 3: Net-(U10A-+) -> Net-(U10-SW)
- U10 pad 4: /Analog Audio/-4.5V -> GND
- U10 pad 5: Net-(U10B-+) -> Net-(U10-FB)
- U10 pad 6: Net-(U10B--) -> Net-(U10-COMP)
- U10 pad 7: Net-(U10B--) -> Net-(U10-EN)
- U10 pad 8: /Analog Audio/+4.5V -> Net-(U10-SS/PG)
- U12 pad 4: /PSU/D- -> /DSP/D-
- U12 pad 5: /PSU/VBUS -> /DSP/VBUS
- U12 pad 6: /PSU/D+ -> /DSP/D+
- U14 pad 1: Net-(U14A--) -> /PSU/+9V
- U14 pad 2: Net-(U14A--) -> /PSU/+9V
- U14 pad 3: Net-(U14A-+) -> Net-(U14-UVLO)
- U14 pad 4: /Analog Audio/-4.5V -> unconnected-(U14-NC-Pad4)
- U14 pad 5: Net-(U14B-+) -> Net-(U14-OVP)
- U14 pad 6: Net-(U14B--) -> unconnected-(U14-MODE-Pad6)
- U14 pad 7: Net-(U14B--) -> unconnected-(U14-SHDN_N-Pad7)
- U14 pad 8: /Analog Audio/+4.5V -> PowerPad
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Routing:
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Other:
- board size 110 x 85 mm -> 100 x 85 mm
